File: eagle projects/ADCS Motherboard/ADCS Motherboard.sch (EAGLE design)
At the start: 145 parts, among them J1 HDR_10_EZFET_DEBUGGER, J11 CNC_3221-10-0300-00, J2A 832-10-012-10-005000, J2B 832-10-012-10-005000, J5 CNC_3221-10-0300-00, J7 TE-1734829-3, Q1 BSR802NL6327HTSA1, U1 MSP430F5529IPN, U10 TSV991AILT, U2 TSV991AILT, U3 ADS7841E_2K5, U4 TSV991AILT, U5 DMC4050SSDQ-13, U6 BNO055, U7 HMC1053, U9 BMX160, Y1 32.768kHz, Y2 CSTCR4M00G15L99, Y3 32.768kHz

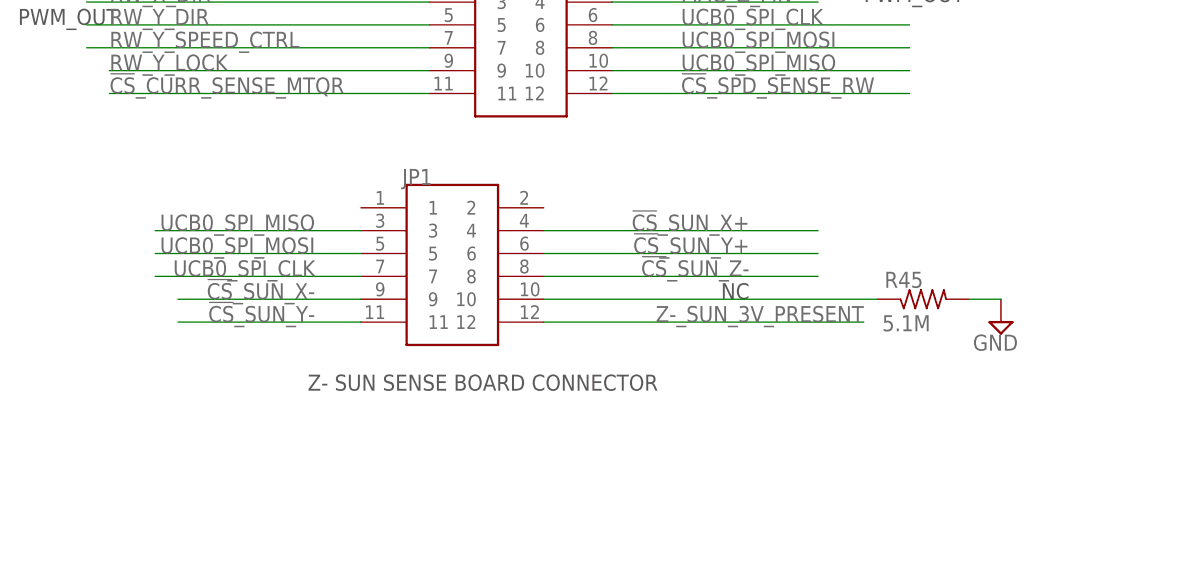
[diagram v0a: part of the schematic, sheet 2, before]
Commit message: Finished updating connectors of mother board
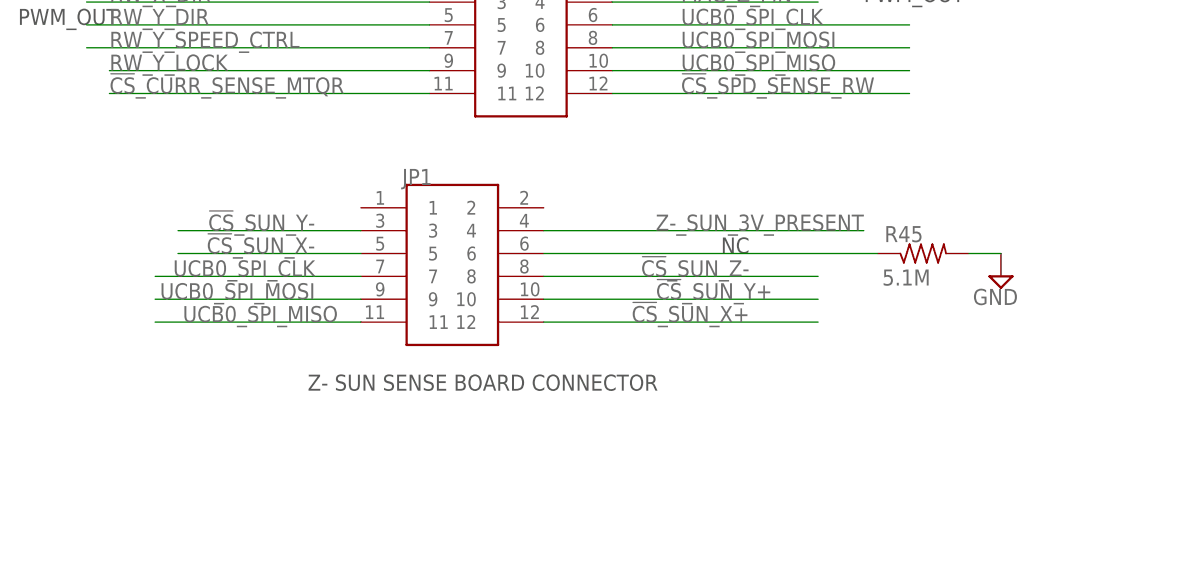
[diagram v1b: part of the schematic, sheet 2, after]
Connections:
- net !CS!_SUN_X+: now also JP1.12; no longer JP1.4
- net !CS!_SUN_X-: now also JP1.5; no longer JP1.9
- net !CS!_SUN_Y+: now also JP1.10; no longer JP1.6
- net !CS!_SUN_Y-: now also JP1.3; no longer JP1.11
- net N$58: now also JP1.6; no longer JP1.10
- net UCB0_SPI_MISO: now also JP1.11; no longer JP1.3
- net UCB0_SPI_MOSI: now also JP1.9; no longer JP1.5
- net Z-_SUN_3V_PRESENT: now also JP1.4; no longer JP1.12
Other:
- moved on the sheet: R45

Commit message: Finished all new connectors
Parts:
- removed J11: CNC_3221-10-0300-00, my_library:CNC_3221-10-0300-00
- removed JP4: (no value), my_library:PINHD-1X6
- added J3: 832-10-012-10-005000, 832-10-012-10-005000:832-10-012-10-005000
- added J8: 830-10-006-20-005000, 830-10-006-20-005000:830-10-006-20-005000
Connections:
- net !CS!_SUN_Z+: now also J8.3; no longer JP4.4
- net +3V3: now also J3.7, J8.6; no longer J11.7, JP4.1
- net ACT_BRD_3V_PRESENT: now also J3.4; no longer J11.4
- net ACT_BRD_5V_SHIFTED: now also J3.2; no longer J11.2
- net GND: now also J8.1; no longer JP4.6
- net MSP430_ACTIVE: now also J3.10; no longer J11.10
- net MSP_OBC_RESET: now also J3.5; no longer J11.5
- net RESERVED_1: now also J3.6; no longer J11.6
- net RESERVED_2: now also J3.8; no longer J11.8
- net UCA0RXD: now also J3.1; no longer J11.1
- net UCA0TXD: now also J3.3; no longer J11.3
- net UCB0_SPI_CLK: now also J8.2; no longer JP4.5
- net UCB0_SPI_MISO: now also J8.5; no longer JP4.2
- net UCB0_SPI_MOSI: now also J8.4; no longer JP4.3
- net Z-_SUN_3V_PRESENT: now also J3.9; no longer J11.9
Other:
- moved on the sheet: LED1, R4, R5, R8

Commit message: Updated footprint names
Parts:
- renumbered J2A to JP2A, J2B to JP2B
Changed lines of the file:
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@@
 <part name="SUPPLY70" library="supply2" library_urn="urn:adsk.eagle:library:372" deviceset="GND" device=""/>
 <part name="JP1" library="832-10-012-10-005000" deviceset="832-10-012-10-005000" device=""/>
-<part name="J2A" library="832-10-012-10-005000" deviceset="832-10-012-10-005000" device=""/>
-<part name="J2B" library="832-10-012-10-005000" deviceset="832-10-012-10-005000" device=""/>
+<part name="JP2A" library="832-10-012-10-005000" deviceset="832-10-012-10-005000" device=""/>
+<part name="JP2B" library="832-10-012-10-005000" deviceset="832-10-012-10-005000" device=""/>
 <part name="R45" library="rcl" library_urn="urn:adsk.eagle:library:334" deviceset="R-US_" device="R0402" package3d_urn="urn:adsk.eagle:package:23547/3" value="5.1M"/>
 <part name="SUPPLY9" library="supply2" library_urn="urn:adsk.eagle:library:372" deviceset="GND" device=""/>
@@
 <attribute name="NAME" x="47.76" y="154.94" size="1.778" layer="95"/>
 </instance>
-<instance part="J2A" gate="G$1" x="60.96" y="195.58" smashed="yes">
+<instance part="JP2A" gate="G$1" x="60.96" y="195.58" smashed="yes">
 <attribute name="NAME" x="55.38" y="205.74" size="1.778" layer="95"/>
 </instance>
-<instance part="J2B" gate="G$1" x="60.96" y="172.72" smashed="yes">
+<instance part="JP2B" gate="G$1" x="60.96" y="172.72" smashed="yes">
 <attribute name="NAME" x="55.38" y="182.88" size="1.778" layer="95"/>
 </instance>
@@
 <wire x1="71.12" y1="172.72" x2="104.14" y2="172.72" width="0.1524" layer="91"/>
 <label x="78.74" y="172.72" size="1.778" layer="95"/>
-<pinref part="J2B" gate="G$1" pin="6"/>
+<pinref part="JP2B" gate="G$1" pin="6"/>
 </segment>
 <segment>
@@
 <wire x1="71.12" y1="167.64" x2="104.14" y2="167.64" width="0.1524" layer="91"/>
 <label x="78.74" y="167.64" size="1.778" layer="95"/>
-<pinref part="J2B" gate="G$1" pin="10"/>
+<pinref part="JP2B" gate="G$1" pin="10"/>
 </segment>
 <segment>
@@
 <wire x1="71.12" y1="170.18" x2="104.14" y2="170.18" width="0.1524" layer="91"/>
 <label x="78.74" y="170.18" size="1.778" layer="95"/>
-<pinref part="J2B" gate="G$1" pin="8"/>
+<pinref part="JP2B" gate="G$1" pin="8"/>
 </segment>
 <segment>
@@
 <wire x1="71.12" y1="195.58" x2="93.98" y2="195.58" width="0.1524" layer="91"/>
 <label x="78.74" y="195.58" size="1.778" layer="95"/>
-<pinref part="J2A" gate="G$1" pin="6"/>
+<pinref part="JP2A" gate="G$1" pin="6"/>
 </segment>
 </net>
@@
 <wire x1="93.98" y1="190.5" x2="71.12" y2="190.5" width="0.1524" layer="91"/>
 <label x="78.74" y="190.5" size="1.778" layer="95"/>
-<pinref part="J2A" gate="G$1" pin="10"/>
+<pinref part="JP2A" gate="G$1" pin="10"/>
 </segment>
 </net>
@@
 <wire x1="71.12" y1="187.96" x2="93.98" y2="187.96" width="0.1524" layer="91"/>
 <label x="78.74" y="187.96" size="1.778" layer="95"/>
-<pinref part="J2A" gate="G$1" pin="12"/>
+<pinref part="JP2A" gate="G$1" pin="12"/>
 </segment>
 </net>
@@
 <wire x1="71.12" y1="177.8" x2="93.98" y2="177.8" width="0.1524" layer="91"/>
 <label x="78.74" y="177.8" size="1.778" layer="95"/>
-<pinref part="J2B" gate="G$1" pin="2"/>
+<pinref part="JP2B" gate="G$1" pin="2"/>
 </segment>
 </net>
@@
 <wire x1="71.12" y1="175.26" x2="93.98" y2="175.26" width="0.1524" layer="91"/>
 <label x="78.74" y="175.26" size="1.778" layer="95"/>
-<pinref part="J2B" gate="G$1" pin="4"/>
+<pinref part="JP2B" gate="G$1" pin="4"/>
 </segment>
 </net>
@@
 <wire x1="71.12" y1="193.04" x2="93.98" y2="193.04" width="0.1524" layer="91"/>
 <label x="78.74" y="193.04" size="1.778" layer="95"/>
-<pinref part="J2A" gate="G$1" pin="8"/>
+<pinref part="JP2A" gate="G$1" pin="8"/>
 </segment>
 </net>
@@
 <wire x1="50.8" y1="200.66" x2="15.24" y2="200.66" width="0.1524" layer="91"/>
 <label x="15.24" y="200.66" size="1.778" layer="95"/>
-<pinref part="J2A" gate="G$1" pin="1"/>
+<pinref part="JP2A" gate="G$1" pin="1"/>
 </segment>
 </net>
@@
 <wire x1="71.12" y1="200.66" x2="109.22" y2="200.66" width="0.1524" layer="91"/>
 <label x="78.74" y="200.66" size="1.778" layer="95"/>
-<pinref part="J2A" gate="G$1" pin="2"/>
+<pinref part="JP2A" gate="G$1" pin="2"/>
 </segment>
 </net>
@@
 <label x="15.24" y="170.18" size="1.778" layer="95"/>
 <wire x1="50.8" y1="170.18" x2="12.7" y2="170.18" width="0.1524" layer="91"/>
-<pinref part="J2B" gate="G$1" pin="7"/>
+<pinref part="JP2B" gate="G$1" pin="7"/>
 </segment>
 </net>
@@
 <wire x1="50.8" y1="195.58" x2="25.4" y2="195.58" width="0.1524" layer="91"/>
 <label x="22.86" y="195.58" size="1.778" layer="95"/>
-<pinref part="J2A" gate="G$1" pin="5"/>
+<pinref part="JP2A" gate="G$1" pin="5"/>
 </segment>
 </net>
@@
 <segment>
 <label x="22.86" y="190.5" size="1.778" layer="95"/>
-<pinref part="J2A" gate="G$1" pin="9"/>
+<pinref part="JP2A" gate="G$1" pin="9"/>
 <wire x1="50.8" y1="190.5" x2="25.4" y2="190.5" width="0.1524" layer="91"/>
 <junction x="50.8" y="190.5"/>
@@
 <wire x1="50.8" y1="198.12" x2="22.86" y2="198.12" width="0.1524" layer="91"/>
 <label x="22.86" y="198.12" size="1.778" layer="95"/>
-<pinref part="J2A" gate="G$1" pin="3"/>
+<pinref part="JP2A" gate="G$1" pin="3"/>
 </segment>
 </net>
@@
 <wire x1="50.8" y1="172.72" x2="12.7" y2="172.72" width="0.1524" layer="91"/>
 <label x="15.24" y="172.72" size="1.778" layer="95"/>
-<pinref part="J2B" gate="G$1" pin="5"/>
+<pinref part="JP2B" gate="G$1" pin="5"/>
 </segment>
 </net>
@@
 <label x="15.24" y="175.26" size="1.778" layer="95"/>
 <wire x1="50.8" y1="175.26" x2="12.7" y2="175.26" width="0.1524" layer="91"/>
-<pinref part="J2B" gate="G$1" pin="3"/>
+<pinref part="JP2B" gate="G$1" pin="3"/>
 </segment>
 </net>
@@
 <wire x1="50.8" y1="177.8" x2="15.24" y2="177.8" width="0.1524" layer="91"/>
 <label x="15.24" y="177.8" size="1.778" layer="95"/>
-<pinref part="J2B" gate="G$1" pin="1"/>
+<pinref part="JP2B" gate="G$1" pin="1"/>
 </segment>
 </net>
@@
 <wire x1="50.8" y1="165.1" x2="15.24" y2="165.1" width="0.1524" layer="91"/>
 <label x="15.24" y="165.1" size="1.778" layer="95"/>
-<pinref part="J2B" gate="G$1" pin="11"/>
+<pinref part="JP2B" gate="G$1" pin="11"/>
 </segment>
 </net>
@@
 <wire x1="50.8" y1="193.04" x2="22.86" y2="193.04" width="0.1524" layer="91"/>
 <label x="22.86" y="193.04" size="1.778" layer="95"/>
-<pinref part="J2A" gate="G$1" pin="7"/>
+<pinref part="JP2A" gate="G$1" pin="7"/>
 </segment>
 </net>
@@
 <wire x1="50.8" y1="187.96" x2="22.86" y2="187.96" width="0.1524" layer="91"/>
 <label x="22.86" y="187.96" size="1.778" layer="95"/>
-<pinref part="J2A" gate="G$1" pin="11"/>
+<pinref part="JP2A" gate="G$1" pin="11"/>
 </segment>
 </net>
@@
 <wire x1="15.24" y1="167.64" x2="50.8" y2="167.64" width="0.1524" layer="91"/>
 <label x="15.24" y="167.64" size="1.778" layer="95"/>
-<pinref part="J2B" gate="G$1" pin="9"/>
+<pinref part="JP2B" gate="G$1" pin="9"/>
 </segment>
 </net>
@@
 <wire x1="71.12" y1="165.1" x2="104.14" y2="165.1" width="0.1524" layer="91"/>
 <label x="78.74" y="165.1" size="1.778" layer="95"/>
-<pinref part="J2B" gate="G$1" pin="12"/>
+<pinref part="JP2B" gate="G$1" pin="12"/>
 </segment>
 </net>
@@
 <pinref part="R55" gate="G$1" pin="2"/>
 <wire x1="71.12" y1="198.12" x2="111.76" y2="198.12" width="0.1524" layer="91"/>
-<pinref part="J2A" gate="G$1" pin="4"/>
-</segment>
-</net>
+<pinref part="JP2A" gate="G$1" pin="4"/>
+</segment>
+</net>

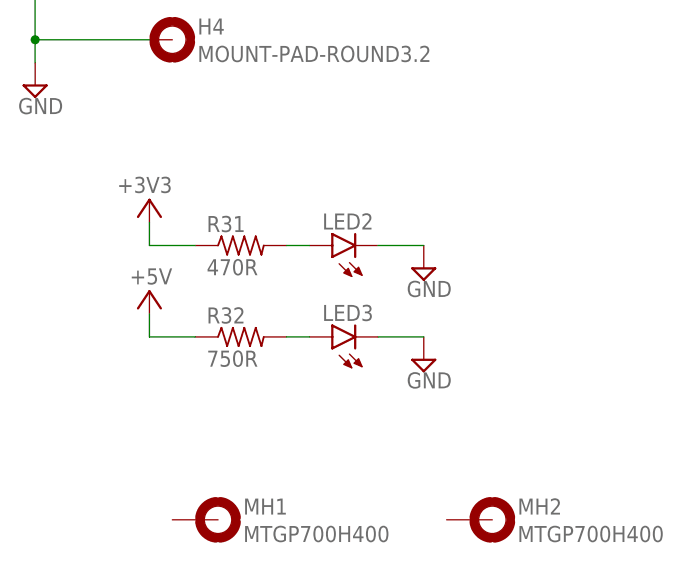
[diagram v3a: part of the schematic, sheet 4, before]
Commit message: Removed LEDs from MOBO
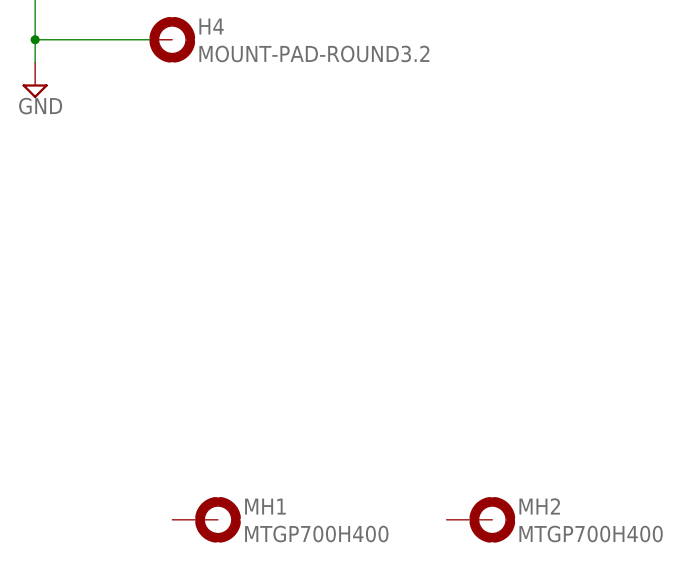
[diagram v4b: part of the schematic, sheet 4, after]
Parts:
- removed LED1, LED2, LED3: (no value), led:LEDCHIP-LED0603
- removed R31, R8: 470R, rcl:R-US_R0603
- removed R32: 750R, rcl:R-US_R0603
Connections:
- removed net N$4: LED1.A, R8.2
- removed net N$5: LED2.A, R31.2
- removed net N$6: LED3.A, R32.2
- net +3V3: no longer R31.1
- net +5V: no longer R32.1
- net GND: no longer LED1.C, LED2.C, LED3.C
- net MSP430_ACTIVE: no longer J3.10, R8.1
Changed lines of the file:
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@@
 <part name="SUPPLY11" library="supply2" library_urn="urn:adsk.eagle:library:372" deviceset="GND" device=""/>
 <part name="S1" library="my_library" library_urn="urn:adsk.eagle:library:22876504" deviceset="10-XX" device="" package3d_urn="urn:adsk.eagle:package:24526167/2" value="RST"/>
-<part name="SUPPLY13" library="supply2" library_urn="urn:adsk.eagle:library:372" deviceset="GND" device=""/>
-<part name="R8" library="rcl" library_urn="urn:adsk.eagle:library:334" deviceset="R-US_" device="R0603" package3d_urn="urn:adsk.eagle:package:23555/3" value="470R"/>
-<part name="LED1" library="led" library_urn="urn:adsk.eagle:library:259" deviceset="LED" device="CHIP-LED0603" package3d_urn="urn:adsk.eagle:package:15819/3"/>
-<part name="LED2" library="led" library_urn="urn:adsk.eagle:library:259" deviceset="LED" device="CHIP-LED0603" package3d_urn="urn:adsk.eagle:package:15819/3"/>
-<part name="LED3" library="led" library_urn="urn:adsk.eagle:library:259" deviceset="LED" device="CHIP-LED0603" package3d_urn="urn:adsk.eagle:package:15819/3"/>
-<part name="R31" library="rcl" library_urn="urn:adsk.eagle:library:334" deviceset="R-US_" device="R0603" package3d_urn="urn:adsk.eagle:package:23555/3" value="470R"/>
-<part name="R32" library="rcl" library_urn="urn:adsk.eagle:library:334" deviceset="R-US_" device="R0603" package3d_urn="urn:adsk.eagle:package:23555/3" value="750R"/>
-<part name="SUPPLY19" library="supply2" library_urn="urn:adsk.eagle:library:372" deviceset="GND" device=""/>
-<part name="SUPPLY25" library="supply2" library_urn="urn:adsk.eagle:library:372" deviceset="GND" device=""/>
-<part name="+3V4" library="supply1" library_urn="urn:adsk.eagle:library:371" deviceset="+3V3" device=""/>
-<part name="P+2" library="supply1" library_urn="urn:adsk.eagle:library:371" deviceset="+5V" device=""/>
 <part name="TP1" library="my_library" library_urn="urn:adsk.eagle:library:22876504" deviceset="TESTPOINT" device="" package3d_urn="urn:adsk.eagle:package:24605432/3"/>
 <part name="TP2" library="my_library" library_urn="urn:adsk.eagle:library:22876504" deviceset="TESTPOINT" device="" package3d_urn="urn:adsk.eagle:package:24605432/3"/>
@@
 <attribute name="VALUE" x="229.235" y="67.945" size="1.778" layer="96"/>
 </instance>
-<instance part="SUPPLY13" gate="GND" x="226.06" y="60.96" smashed="yes">
-<attribute name="VALUE" x="224.155" y="57.785" size="1.778" layer="96"/>
-</instance>
-<instance part="R8" gate="G$1" x="210.82" y="63.5" smashed="yes">
-<attribute name="NAME" x="207.01" y="64.9986" size="1.778" layer="95"/>
-<attribute name="VALUE" x="207.01" y="60.198" size="1.778" layer="96"/>
-</instance>
-<instance part="LED1" gate="G$1" x="218.44" y="63.5" smashed="yes" rot="R90">
-<attribute name="NAME" x="223.012" y="67.056" size="1.778" layer="95" rot="R180"/>
-<attribute name="VALUE" x="223.012" y="69.215" size="1.778" layer="96" rot="R180"/>
-</instance>
 <instance part="+3V2" gate="G$1" x="139.7" y="71.12" smashed="yes">
 <attribute name="VALUE" x="142.24" y="71.12" size="1.778" layer="96" rot="R180"/>
@@
 </segment>
 <segment>
-<pinref part="LED1" gate="G$1" pin="C"/>
-<pinref part="SUPPLY13" gate="GND" pin="GND"/>
-<wire x1="223.52" y1="63.5" x2="226.06" y2="63.5" width="0.1524" layer="91"/>
-</segment>
-<segment>
 <pinref part="J1" gate="G$1" pin="GND"/>
 <wire x1="208.28" y1="160.02" x2="213.36" y2="160.02" width="0.1524" layer="91" grouprefs="EZFET_DEBUGGER_HEADER"/>
@@
 </segment>
 </net>
-<net name="N$4" class="0">
-<segment>
-<pinref part="LED1" gate="G$1" pin="A"/>
-<pinref part="R8" gate="G$1" pin="2"/>
-</segment>
-</net>
 <net name="TEST/SBWTCK" class="0">
 <segment>
@@
 </segment>
 </net>
-<net name="MSP430_ACTIVE" class="0">
-<segment>
-<wire x1="190.5" y1="63.5" x2="205.74" y2="63.5" width="0.1524" layer="91"/>
-<pinref part="R8" gate="G$1" pin="1"/>
-<label x="193.04" y="63.5" size="1.778" layer="95"/>
-<pinref part="J3" gate="G$1" pin="10"/>
-</segment>
-</net>
 <net name="RW_Z_LOCK" class="0">
 <segment>
@@
 <attribute name="VALUE" x="124.714" y="7.6962" size="1.778" layer="96"/>
 </instance>
-<instance part="LED2" gate="G$1" x="40.64" y="40.64" smashed="yes" rot="R90" grouprefs="POWER_INDICATOR_LEDS">
-<attribute name="NAME" x="45.212" y="44.196" size="1.778" layer="95" rot="R180"/>
-<attribute name="VALUE" x="45.212" y="46.355" size="1.778" layer="96" rot="R180"/>
-</instance>
-<instance part="LED3" gate="G$1" x="40.64" y="30.48" smashed="yes" rot="R90" grouprefs="POWER_INDICATOR_LEDS">
-<attribute name="NAME" x="45.212" y="34.036" size="1.778" layer="95" rot="R180"/>
-<attribute name="VALUE" x="45.212" y="36.195" size="1.778" layer="96" rot="R180"/>
-</instance>
-<instance part="R31" gate="G$1" x="30.48" y="40.64" smashed="yes" grouprefs="POWER_INDICATOR_LEDS">
-<attribute name="NAME" x="26.67" y="42.1386" size="1.778" layer="95"/>
-<attribute name="VALUE" x="26.67" y="37.338" size="1.778" layer="96"/>
-</instance>
-<instance part="R32" gate="G$1" x="30.48" y="30.48" smashed="yes" grouprefs="POWER_INDICATOR_LEDS">
-<attribute name="NAME" x="26.67" y="31.9786" size="1.778" layer="95"/>
-<attribute name="VALUE" x="26.67" y="27.178" size="1.778" layer="96"/>
-</instance>
-<instance part="SUPPLY19" gate="GND" x="50.8" y="27.94" smashed="yes" grouprefs="POWER_INDICATOR_LEDS">
-<attribute name="VALUE" x="48.895" y="24.765" size="1.778" layer="96"/>
-</instance>
-<instance part="SUPPLY25" gate="GND" x="50.8" y="38.1" smashed="yes" grouprefs="POWER_INDICATOR_LEDS">
-<attribute name="VALUE" x="48.895" y="34.925" size="1.778" layer="96"/>
-</instance>
-<instance part="+3V4" gate="G$1" x="20.32" y="45.72" smashed="yes" grouprefs="POWER_INDICATOR_LEDS">
-<attribute name="VALUE" x="22.86" y="48.26" size="1.778" layer="96" rot="R180"/>
-</instance>
-<instance part="P+2" gate="1" x="20.32" y="35.56" smashed="yes" grouprefs="POWER_INDICATOR_LEDS">
-<attribute name="VALUE" x="22.86" y="38.1" size="1.778" layer="96" rot="R180"/>
-</instance>
 <instance part="H1" gate="G$1" x="22.86" y="93.98" smashed="yes" grouprefs="STANDOFF_MOUTING_HOLES">
 <attribute name="NAME" x="25.654" y="94.5642" size="1.778" layer="95"/>
@@
 <net name="+3V3" class="0">
 <segment>
-<pinref part="+3V4" gate="G$1" pin="+3V3"/>
-<wire x1="20.32" y1="43.18" x2="20.32" y2="40.64" width="0.1524" layer="91" grouprefs="POWER_INDICATOR_LEDS"/>
-<pinref part="R31" gate="G$1" pin="1"/>
-<wire x1="20.32" y1="40.64" x2="25.4" y2="40.64" width="0.1524" layer="91" grouprefs="POWER_INDICATOR_LEDS"/>
-</segment>
-<segment>
 <pinref part="R41" gate="G$1" pin="2"/>
 <pinref part="+3V9" gate="G$1" pin="+3V3"/>
@@
 <net name="GND" class="0">
 <segment>
-<pinref part="SUPPLY25" gate="GND" pin="GND"/>
-<pinref part="LED2" gate="G$1" pin="C"/>
-<wire x1="50.8" y1="40.64" x2="45.72" y2="40.64" width="0.1524" layer="91" grouprefs="POWER_INDICATOR_LEDS"/>
-</segment>
-<segment>
-<pinref part="LED3" gate="G$1" pin="C"/>
-<pinref part="SUPPLY19" gate="GND" pin="GND"/>
-<wire x1="45.72" y1="30.48" x2="50.8" y2="30.48" width="0.1524" layer="91" grouprefs="POWER_INDICATOR_LEDS"/>
-</segment>
-<segment>
 <pinref part="SUPPLY15" gate="GND" pin="GND"/>
 <pinref part="U6" gate="G$1" pin="COM3/I2C_ADDR"/>
@@
 </segment>
 </net>
-<net name="+5V" class="0">
-<segment>
-<pinref part="P+2" gate="1" pin="+5V"/>
-<wire x1="20.32" y1="33.02" x2="20.32" y2="30.48" width="0.1524" layer="91" grouprefs="POWER_INDICATOR_LEDS"/>
-<pinref part="R32" gate="G$1" pin="1"/>
-<wire x1="20.32" y1="30.48" x2="25.4" y2="30.48" width="0.1524" layer="91" grouprefs="POWER_INDICATOR_LEDS"/>
-</segment>
-</net>
-<net name="N$5" class="0">
-<segment>
-<pinref part="R31" gate="G$1" pin="2"/>
-<pinref part="LED2" gate="G$1" pin="A"/>
-<wire x1="35.56" y1="40.64" x2="38.1" y2="40.64" width="0.1524" layer="91" grouprefs="POWER_INDICATOR_LEDS"/>
-</segment>
-</net>
-<net name="N$6" class="0">
-<segment>
-<pinref part="R32" gate="G$1" pin="2"/>
-<pinref part="LED3" gate="G$1" pin="A"/>
-<wire x1="35.56" y1="30.48" x2="38.1" y2="30.48" width="0.1524" layer="91" grouprefs="POWER_INDICATOR_LEDS"/>
-</segment>
-</net>
